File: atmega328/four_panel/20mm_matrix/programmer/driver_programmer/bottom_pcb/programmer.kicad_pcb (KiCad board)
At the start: 2 copper layers, 65 x 60 mm, 6 parts, among them P1 CONN_2, P2 CONN_3X2, P3 CONN_3X2, P4 CONN_3X2, P5 CONN_2, P6 CONN_3X2

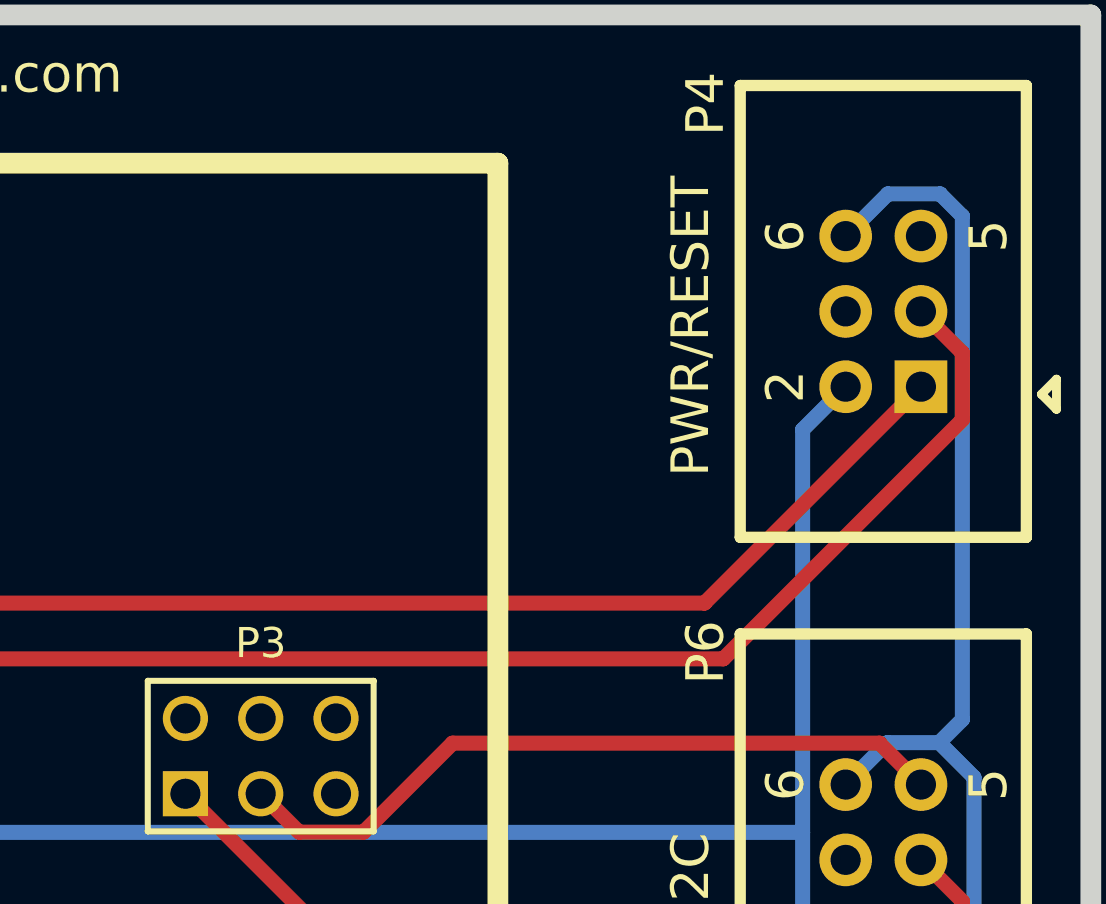
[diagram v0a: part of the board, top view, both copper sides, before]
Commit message: Created gerber files for test_arena and programmer pcbs. Fixed of few small errors.
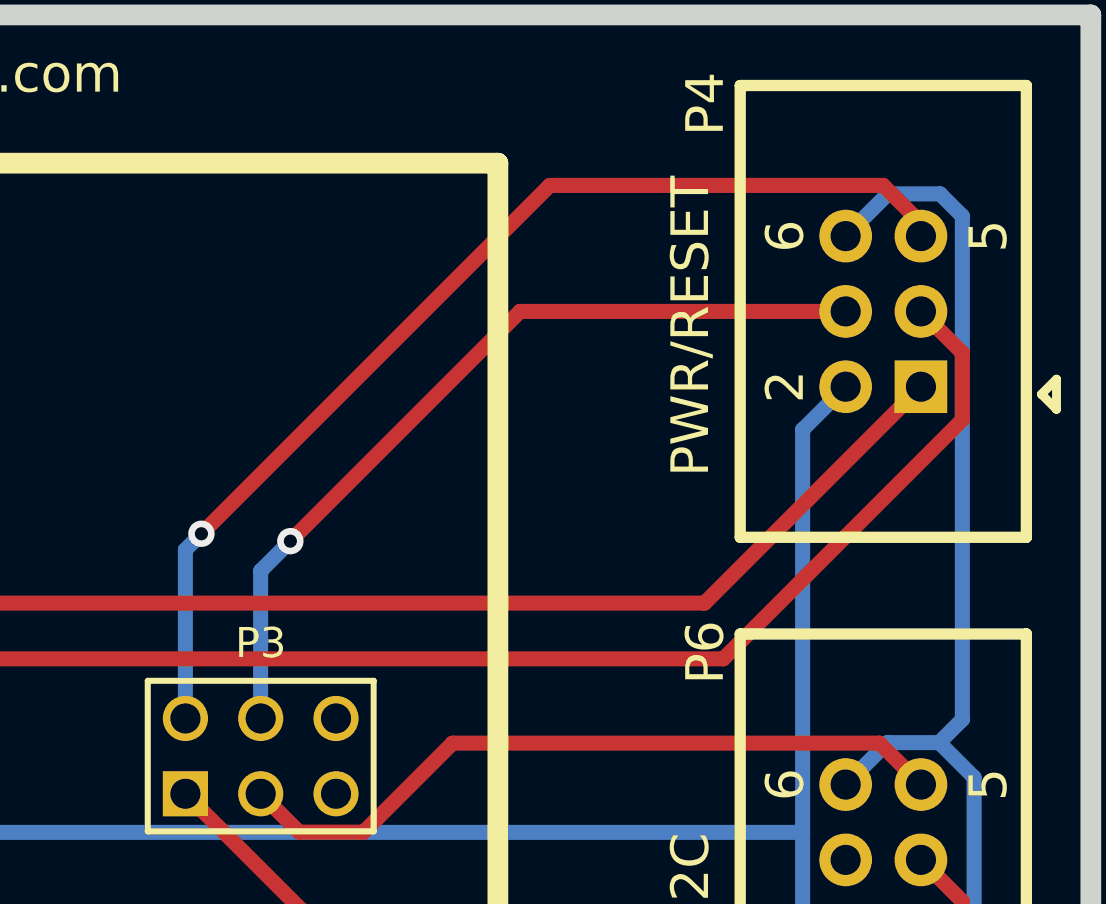
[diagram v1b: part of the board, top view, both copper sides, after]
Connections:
- P3 pad 2: /RST_3 -> /~RST_3
- P3 pad 4: /RST_4 -> /~RST_4
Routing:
- net /~RST_3: track 0.00 -> 36.6 mm, vias 0 -> 1
- net /~RST_4: track 0.00 -> 28.3 mm, vias 0 -> 1
